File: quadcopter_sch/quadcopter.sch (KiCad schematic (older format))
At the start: 19 parts, among them U1 WeAct_Black_Pill_V3.0(STM32F4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, U10 HAKRC_BLHeli_32Bit_35A_2-5S_E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, U11 iFlight_XING-E_2207_2450KV, U12 iFlight_XING-E_2207_2450KV, U13 iFlight_XING-E_2207_2450KV, U14 iFlight_XING-E_2207_2450KV, U2 ST-LINK, U3 4S_Lipo_Battery, U4 Matek_PDB-XT60_3-4S, U5 SparkFun_9Dof_IMU_Breakout-IC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

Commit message: Display joystick value
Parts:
- removed U2: ST-LINK, symbol quadcopter-rescue:ST-LINK
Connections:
- net SWCLK is gone; now on net TIM5_CH4: U1.~ (VB)
- net SWDIO is gone; now on net TIM5_CH4: U1.~ (VB)
- new net: U3.~ (-), U4.~ (VCC)
- no-connect marks 36 -> 34
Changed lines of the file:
@@
 Text GLabel 1675 3375 0    50   Input ~ 0
 SPI1_MOSI
-$Comp
-L quadcopter-rescue:ST-LINK U2
-U 1 1 60D8FF02
-P 2725 1325
-F 0 "U2" H 3050 875 50  0000 R CNN
-F 1 "ST-LINK" H 3050 950 50  0000 R CNN
-F 2 "" H 2125 1100 50  0001 C CNN
-F 3 "" H 2125 1100 50  0001 C CNN
-	1    2725 1325
-	-1   0    0    1
-$EndComp
-Wire Wire Line
-	2475 1725 2475 1425
-Wire Wire Line
-	2575 1725 2575 1425
-Wire Wire Line
-	2675 1425 2675 1725
-Wire Wire Line
-	2775 1425 2775 1725
-NoConn ~ 2875 1425
-NoConn ~ 2975 1425
-Text Label 2575 1700 1    50   ~ 0
-SWCLK
-Text Label 2675 1700 1    50   ~ 0
-SWDIO
 Wire Wire Line
 	1675 3075 2025 3075

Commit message: Update quadcopter schematic
- add FS-A8S
- rename symbals
- relocation symbals in schematic
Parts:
- removed R1: 470k, symbol Device:R_US
- removed R2: 100k, symbol Device:R_US
- removed R3: 1k, symbol Device:R_US
- removed U10, U8, U9: HAKRC_BLHeli_32Bit_35A_2-5S_ESC, symbol quadcopter-rescue:HAKRC_BLHeli_32Bit_35A_2-5S_ESC
- removed U12, U13, U14: iFlight_XING-E_2207_2450KV, symbol quadcopter-rescue:iFlight_XING-E_2207_2450KV
- removed U3: 4S_Lipo_Battery, symbol quadcopter-rescue:4S_Lipo_Battery
- removed U?: nrf24l01+pa+lna_rf_transceiver_module, symbol quadcopter-rescue:nrf24l01+pa+lna_rf_transceiver_module
- added D2, D3: LED, symbol Device:LED
- added R1, R2, R3: R, symbol Device:R
- added U11, U12, U13: iFlight_XING-E, symbol quadcopter-rescue:iFlight_XING-E
- added U2: FS-A8S, symbol quadcopter-rescue:FS-A8S
- added U3: nrf24l01+_module, symbol quadcopter-rescue:nrf24l01+_module
- added U7, U8, U9: HAKRC_ESC, symbol quadcopter-rescue:HAKRC_ESC
- U1: renamed from U5; value SparkFun_9Dof_IMU_Breakout-ICM-20948(Qwiic) -> ICM20948_module; symbol quadcopter-rescue:SparkFun_9Dof_IMU_Breakout-ICM-20948(Qwiic) -> quadcopter-rescue:ICM20948_module
- U10: renamed from U11; value iFlight_XING-E_2207_2450KV -> iFlight_XING-E; symbol quadcopter-rescue:iFlight_XING-E_2207_2450KV -> quadcopter-rescue:iFlight_XING-E
- U4: value Matek_PDB-XT60_3-4S -> PDB-XT60; symbol quadcopter-rescue:Matek_PDB-XT60_3-4S -> quadcopter-rescue:PDB-XT60
- U5: renamed from U1; value WeAct_Black_Pill_V3.0(STM32F411CEU6) -> STM32F411_module; symbol quadcopter-rescue:WeAct_Black_Pill_V3.0(STM32F411CEU6) -> quadcopter-rescue:STM32F411_module
- U6: renamed from U7; value HAKRC_BLHeli_32Bit_35A_2-5S_ESC -> HAKRC_ESC; symbol quadcopter-rescue:HAKRC_BLHeli_32Bit_35A_2-5S_ESC -> quadcopter-rescue:HAKRC_ESC
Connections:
- net ADC_BAT is gone; now on net USART1_RX: U5.~ (VB)
- net +3V3: now also U3.~ (~CSN); no longer U1.~ (VIN)
- net +5V: now also U1.~ (VIN), U2.~ (VCC)
- net CE: now also U3.~ (~CSN)
- net GND: now also D1.1 (K), D2.1 (K), D3.1 (K), U2.~ (VCC), U3.~ (~CSN), U7.~ (VCC), U8.~ (VCC), U9.~ (VCC)
- net SPI2_CSN: now also U3.~ (~CSN)
- net SPI2_MISO: now also U3.~ (~CSN)
- net SPI2_MOSI: now also U3.~ (~CSN)
- net SPI2_SCK: now also U3.~ (~CSN)
- net TIM2_CH1: now also U8.~ (VCC)
- net TIM2_CH3: now also U7.~ (VCC)
- net TIM5_CH2: now also U9.~ (VCC)
- net VCC: now also U7.~ (VCC), U8.~ (VCC), U9.~ (VCC)
- net BUZZER: now reaches BZ1.1 (-), U5.~ (VB)
- net USART1_RX: now reaches U5.~ (VB)
- net USART1_RX: now also U2.~ (VCC)
- net at D1.2 (A): now also R1.1
- new net: U11.1, U7.~ (VCC)
- new net: U11.2, U7.~ (VCC)
- new net: U11.3, U7.~ (VCC)
- new net: U12.1, U8.~ (VCC)
- new net: U12.2, U8.~ (VCC)
- new net: U12.3, U8.~ (VCC)
- new net: U13.1, U9.~ (VCC)
- new net: U13.2, U9.~ (VCC)
- new net: U13.3, U9.~ (VCC)
- new net: D2.2 (A), R2.1
- new net: D3.2 (A), R3.1
- new net IRQ: U3.~ (~CSN), U5.~ (VB)
- new net LED1: R1.2, U5.~ (VB)
- new net LED2: R2.2, U5.~ (VB)
- new net LED3: R3.2, U5.~ (VB)
- no-connect marks 34 -> 33
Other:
- note added: "IMU"
- note added: "Indicator"
- note added: "MCU"
- note added: "RC receiver"
- note added: "RF transceiver"
- note removed: "IMU (ICM20948)"
- note removed: "MCU Module (STM32F411CEU6)"
- note removed: "Onboard Led"
- note removed: "RF transceiver (nrf24l01)"
- note removed: "Voltage Monitor"
- moved on the sheet: U1, U10, U4, U5, U6

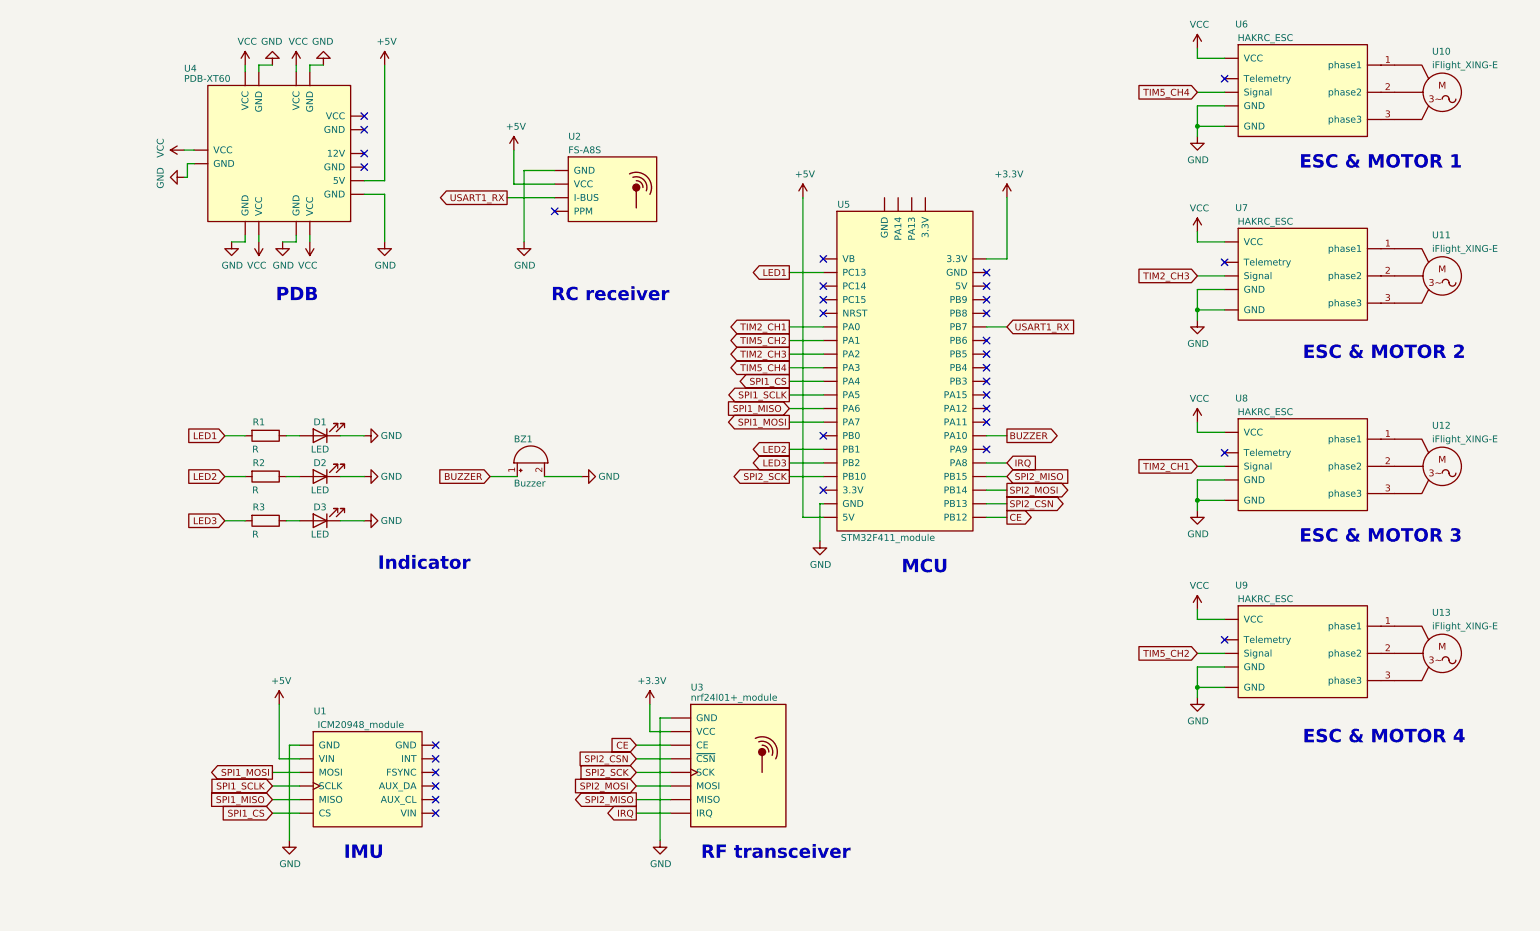
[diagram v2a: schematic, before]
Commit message: Update quadcopter_sck
- add imu_int pin
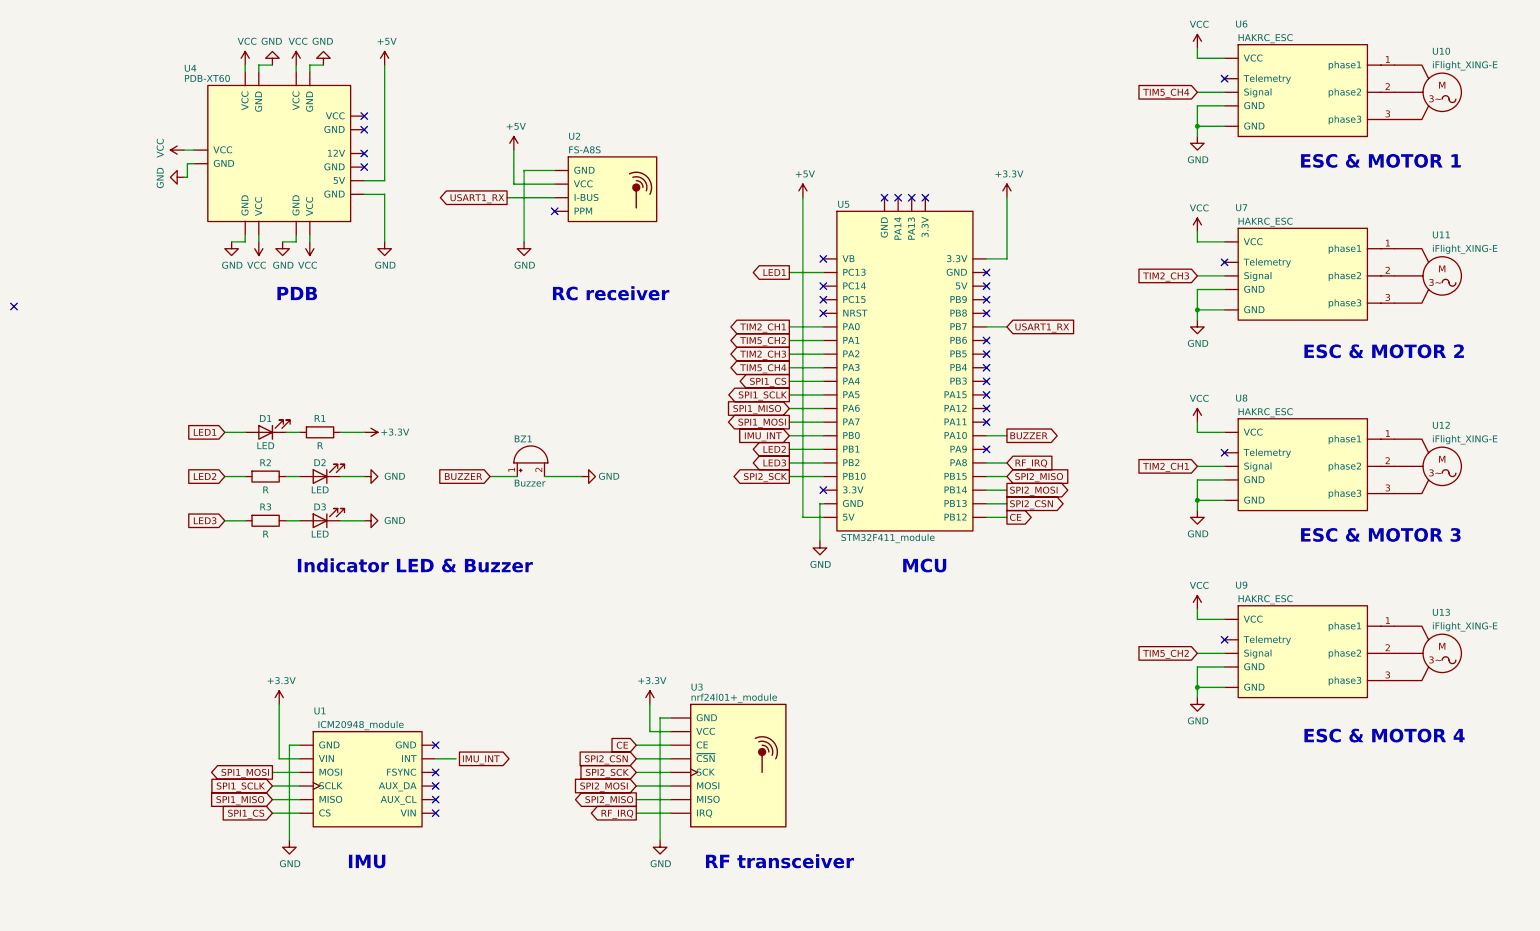
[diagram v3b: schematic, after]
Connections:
- net +3V3: now also R1.1, U1.~ (VIN)
- net +5V: no longer U1.~ (VIN)
- net GND: no longer D1.1 (K)
- net LED1: now also D1.2 (A); no longer R1.2
- removed net IRQ: U3.~ (~CSN), U5.~ (VB)
- new net: D1.1 (K), R1.2
- new net IMU_INT: U5.~ (VB)
- new net RF_IRQ: U3.~ (~CSN), U5.~ (VB)
- no-connect marks 33 -> 36
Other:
- note added: "Indicator LED & Buzzer"
- note removed: "Indicator"
- moved on the sheet: D1, R1
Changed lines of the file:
@@
 Wire Wire Line
 	5725 4400 5725 4675
-$Comp
-L power:+3.3V #PWR017
-U 1 1 60DA15AA
-P 4475 5875
-F 0 "#PWR017" H 4475 5725 50  0001 C CNN
-F 1 "+3.3V" H 4490 6048 50  0000 C CNN
-F 2 "" H 4475 5875 50  0001 C CNN
-F 3 "" H 4475 5875 50  0001 C CNN
-	1    4475 5875
-	1    0    0    -1
-$EndComp
 Wire Wire Line
 	1700 6675 1900 6675
@@
 L power:+3.3V #PWR025
 U 1 1 60DABAF8
-P 7100 2150
-F 0 "#PWR025" H 7100 2000 50  0001 C CNN
-F 1 "+3.3V" H 7115 2323 50  0000 C CNN
-F 2 "" H 7100 2150 50  0001 C CNN
-F 3 "" H 7100 2150 50  0001 C CNN
-	1    7100 2150
-	1    0    0    -1
+P 2375 3875
+F 0 "#PWR025" H 2375 3725 50  0001 C CNN
+F 1 "+3.3V" V 2375 4100 50  0000 C CNN
+F 2 "" H 2375 3875 50  0001 C CNN
+F 3 "" H 2375 3875 50  0001 C CNN
+	1    2375 3875
+	0    1    1    0
 $EndComp
 Wire Wire Line
@@
 Text Notes 1725 2925 0    98   ~ 20
 PDB
-Text Notes 4850 7025 0    98   ~ 20
+Text Notes 4875 7100 0    98   ~ 20
 RF transceiver
-Text Notes 2225 7025 0    98   ~ 20
+Text Notes 2250 7100 0    98   ~ 20
 IMU
 Text Notes 6325 4925 0    98   ~ 20
@@
 Text Notes 9275 3350 0    98   ~ 20
 ESC & MOTOR 2
-NoConn ~ 2900 6275
 NoConn ~ 2900 6375
 NoConn ~ 2900 6475
@@
 NoConn ~ 2900 6175
 Text GLabel 4375 6675 0    50   Output ~ 0
-IRQ
+RF_IRQ
 Wire Wire Line
 	4375 6275 4625 6275
@@
 	4550 5975 4550 6875
 Text GLabel 7100 4100 2    50   Input ~ 0
-IRQ
+RF_IRQ
 Wire Wire Line
 	5500 4100 5750 4100
@@
 	3425 2150 3775 2150
 NoConn ~ 3775 2250
-$Comp
-L power:+5V #PWR01
-U 1 1 61539932
-P 1750 5875
-F 0 "#PWR01" H 1750 5725 50  0001 C CNN
-F 1 "+5V" H 1765 6048 50  0000 C CNN
-F 2 "" H 1750 5875 50  0001 C CNN
-F 3 "" H 1750 5875 50  0001 C CNN
-	1    1750 5875
-	1    0    0    -1
-$EndComp
 Wire Wire Line
 	7100 4100 6950 4100
@@
 Text GLabel 7100 3900 2    50   Output ~ 0
 BUZZER
-NoConn ~ 5750 3900
-Text GLabel 1350 3900 0    50   Input ~ 0
+Text GLabel 1350 3875 0    50   Input ~ 0
 LED1
 $Comp
 L Device:LED D1
 U 1 1 615A225C
-P 2050 3900
-F 0 "D1" H 2050 3800 50  0000 C CNN
-F 1 "LED" H 2050 4000 50  0000 C CNN
-F 2 "" H 2050 3900 50  0001 C CNN
-F 3 "~" H 2050 3900 50  0001 C CNN
-	1    2050 3900
+P 1650 3875
+F 0 "D1" H 1650 3775 50  0000 C CNN
+F 1 "LED" H 1650 3975 50  0000 C CNN
+F 2 "" H 1650 3875 50  0001 C CNN
+F 3 "~" H 1650 3875 50  0001 C CNN
+	1    1650 3875
 	-1   0    0    1
 $EndComp
 Wire Wire Line
-	1800 3900 1900 3900
-$Comp
-L power:GND #PWR05
-U 1 1 615A9400
-P 2375 3900
-F 0 "#PWR05" H 2375 3650 50  0001 C CNN
-F 1 "GND" V 2375 3700 50  0000 C CNN
-F 2 "" H 2375 3900 50  0001 C CNN
-F 3 "" H 2375 3900 50  0001 C CNN
-	1    2375 3900
-	0    -1   -1   0
-$EndComp
-Wire Wire Line
-	2200 3900 2375 3900
-Wire Wire Line
-	1350 3900 1500 3900
+	1800 3875 1900 3875
+Wire Wire Line
+	2200 3875 2375 3875
+Wire Wire Line
+	1350 3875 1500 3875
 $Comp
 L Device:R R1
 U 1 1 615A162E
-P 1650 3900
-F 0 "R1" V 1550 3850 50  0000 C CNN
-F 1 "R" V 1750 3825 50  0000 C CNN
-F 2 "" V 1580 3900 50  0001 C CNN
-F 3 "~" H 1650 3900 50  0001 C CNN
-	1    1650 3900
+P 2050 3875
+F 0 "R1" V 1950 3875 50  0000 C CNN
+F 1 "R" V 2150 3875 50  0000 C CNN
+F 2 "" V 1980 3875 50  0001 C CNN
+F 3 "~" H 2050 3875 50  0001 C CNN
+	1    2050 3875
 	0    1    1    0
 $EndComp
@@
 P 2375 4200
 F 0 "#PWR06" H 2375 3950 50  0001 C CNN
-F 1 "GND" V 2375 4000 50  0000 C CNN
+F 1 "GND" V 2375 3975 50  0000 C CNN
 F 2 "" H 2375 4200 50  0001 C CNN
 F 3 "" H 2375 4200 50  0001 C CNN
@@
 U 1 1 615C8A4C
 P 1650 4200
-F 0 "R2" V 1550 4150 50  0000 C CNN
-F 1 "R" V 1750 4125 50  0000 C CNN
+F 0 "R2" V 1550 4200 50  0000 C CNN
+F 1 "R" V 1750 4200 50  0000 C CNN
 F 2 "" V 1580 4200 50  0001 C CNN
 F 3 "~" H 1650 4200 50  0001 C CNN
@@
 P 2375 4525
 F 0 "#PWR08" H 2375 4275 50  0001 C CNN
-F 1 "GND" V 2375 4325 50  0000 C CNN
+F 1 "GND" V 2375 4300 50  0000 C CNN
 F 2 "" H 2375 4525 50  0001 C CNN
 F 3 "" H 2375 4525 50  0001 C CNN
@@
 U 1 1 615CBF5E
 P 1650 4525
-F 0 "R3" V 1550 4475 50  0000 C CNN
-F 1 "R" V 1750 4450 50  0000 C CNN
+F 0 "R3" V 1550 4525 50  0000 C CNN
+F 1 "R" V 1750 4525 50  0000 C CNN
 F 2 "" V 1580 4525 50  0001 C CNN
 F 3 "~" H 1650 4525 50  0001 C CNN
@@
 Wire Wire Line
 	3700 4200 3975 4200
-Text Notes 2475 4900 0    98   ~ 20
-Indicator
+Text Notes 1875 4925 0    98   ~ 20
+Indicator LED & Buzzer
 Wire Wire Line
 	3475 1800 3475 2050
@@
 	1    0    0    -1
 $EndComp
+Text GLabel 3075 6275 2    50   Output ~ 0
+IMU_INT
+Text GLabel 5500 3900 0    50   Input ~ 0
+IMU_INT
+Wire Wire Line
+	5750 3900 5500 3900
+Wire Wire Line
+	2900 6275 3050 6275
+$Comp
+L power:+3.3V #PWR017
+U 1 1 60DA15AA
+P 4475 5875
+F 0 "#PWR017" H 4475 5725 50  0001 C CNN
+F 1 "+3.3V" H 4490 6048 50  0000 C CNN
+F 2 "" H 4475 5875 50  0001 C CNN
+F 3 "" H 4475 5875 50  0001 C CNN
+	1    4475 5875
+	1    0    0    -1
+$EndComp
+$Comp
+L power:+3.3V #PWR?
+U 1 1 61300712
+P 1750 5875
+F 0 "#PWR?" H 1750 5725 50  0001 C CNN
+F 1 "+3.3V" H 1765 6048 50  0000 C CNN
+F 2 "" H 1750 5875 50  0001 C CNN
+F 3 "" H 1750 5875 50  0001 C CNN
+	1    1750 5875
+	1    0    0    -1
+$EndComp
+$Comp
+L power:+3.3V #PWR?
+U 1 1 61301C24
+P 7100 2150
+F 0 "#PWR?" H 7100 2000 50  0001 C CNN
+F 1 "+3.3V" H 7115 2323 50  0000 C CNN
+F 2 "" H 7100 2150 50  0001 C CNN
+F 3 "" H 7100 2150 50  0001 C CNN
+	1    7100 2150
+	1    0    0    -1
+$EndComp
+NoConn ~ 6200 2150
+NoConn ~ 6300 2150
+NoConn ~ 6400 2150
+NoConn ~ 6500 2150
+NoConn ~ -200 2950
 $EndSCHEMATC
